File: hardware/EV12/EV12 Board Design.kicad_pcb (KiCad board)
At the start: 4 copper layers, 66 x 99.3 mm, 129 parts, among them CN2 Conn_05x02_Female, CN3 Conn_01x06_Female, CN4 Conn_01x06_Female, CN5 Conn_02x05_Male, CN6 Conn_02x05_Male, CN7 Conn_02x05_Male, J1 Conn_01x02_Socket, J10 Conn_01x08_Socket, J2 AudioJack1, J3 Conn_01x06_Socket, J9 USB_C_Receptacle, SW1 TS-1037-A11B3-D2, SW3 TS-1037-A11B3-D2, SW4 SW_Push, SW5 SW_Push, SW6 SW_SPDT, U1 STM32F405RGTx, U11 ESP32-S3-WROOM-1-N8R2, U13 BM14B(0.8)-24DS-0.4V(53), U2 BQ21040DBV, U3 CH340C, U4 USBLC6-2P6, U5 M24C02-RMN6TP, U6 WM8960CGEFL/RV, U7 TPS63060, U8 STM32F072CBTx, Y1 Crystal_GND24

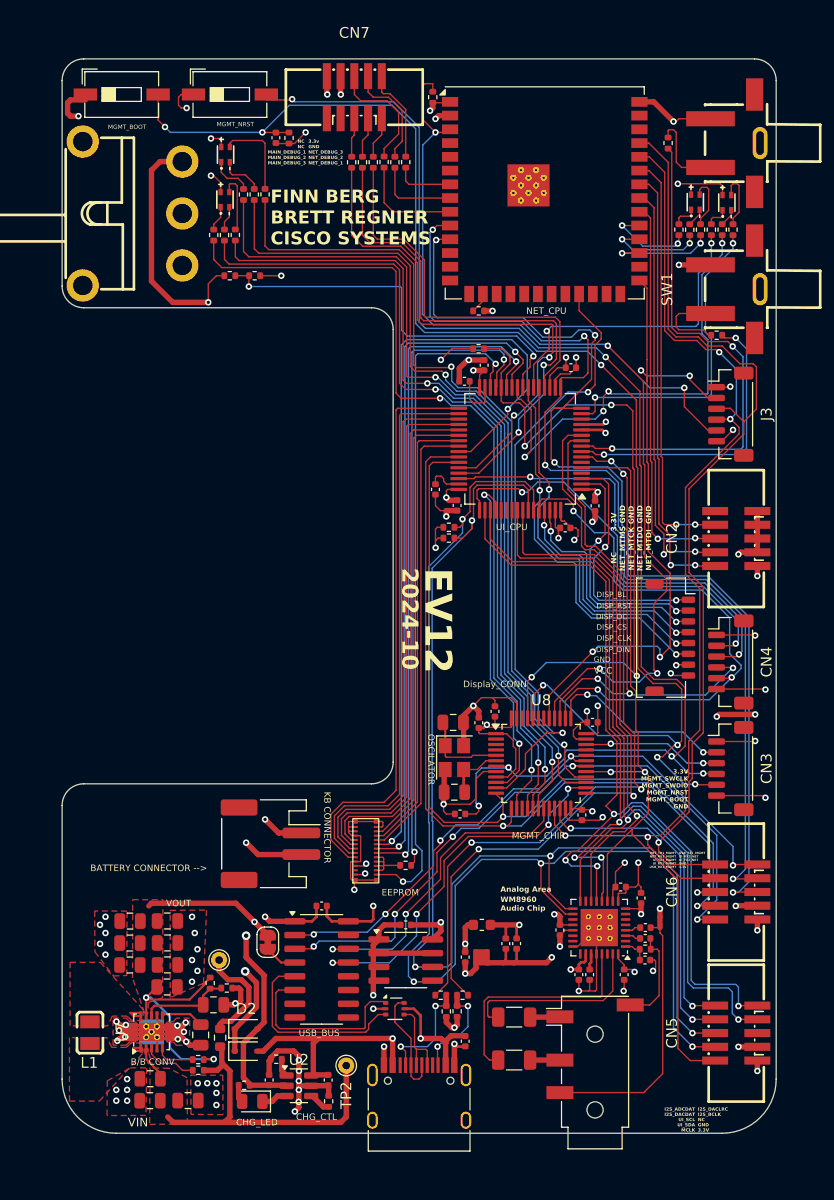
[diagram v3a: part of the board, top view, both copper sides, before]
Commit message: Added some design rules, updated track widths to be between 5 to 15mils except for long power lines
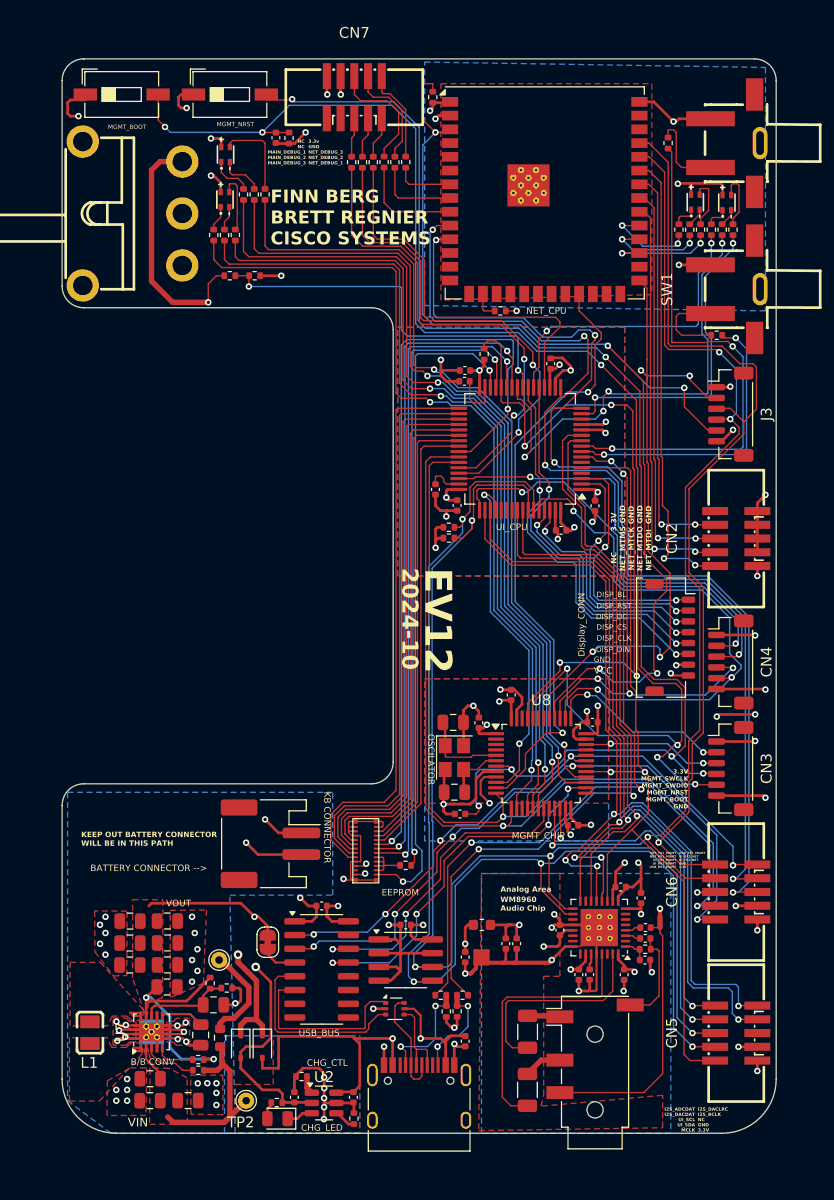
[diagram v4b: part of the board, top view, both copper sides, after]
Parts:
- moved TP2 9.80 mm to (131.0, 142.3)
- moved R27 3.41 mm to (133.8, 142.5)
- moved C29 3.02 mm to (157.0, 141.3), turned to 90 degrees
- moved R22 2.83 mm to (136.1, 140.1)
- moved D1 2.83 mm to (133.9, 144.0)
- moved C2 2.83 mm to (135.5, 142.0)
- moved C21 2.83 mm to (140.9, 142.0)
- moved R26 2.83 mm to (141.0, 143.9)
- moved U2 2.83 mm to (138.2, 142.5)
- moved C26 2.14 mm to (155.5, 104.8)
- moved R32 2.00 mm to (154.5, 69.3)
- moved C11 1.91 mm to (159.2, 74.2), turned to 90 degrees
- moved C14 1.84 mm to (151.2, 74.8), turned to 180 degrees
- moved C30 1.84 mm to (157.0, 135.9), turned to 90 degrees
- moved D2 1.72 mm to (130.5, 137.3), turned to -90 degrees
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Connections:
- CN2 pad 2: /NET_MTDI -> /NET_MTMS
- CN2 pad 4: /NET_MTDO -> /NET_MTCK
- CN2 pad 6: /NET_MTCK -> /NET_MTDO
- CN2 pad 8: /NET_MTMS -> /NET_MTDI
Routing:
- net Net-(U7-VIN): track 34.8 -> 20.7 mm
- net /UI_DEBUG_1: track 49.6 -> 44.3 mm
- net VBUS: track 33.7 -> 38.6 mm
- net Net-(D2-A): track 33.0 -> 37.7 mm
- net GNDA: track 70.7 -> 75.2 mm, vias 7 -> 8
- net /UI_DEBUG_2: track 49.6 -> 45.2 mm
- net /NET_MTMS: track 38.9 -> 42.5 mm
- net /NET_MTDI: track 41.0 -> 37.8 mm
- net Net-(U6-HP_R): track 21.5 -> 24.8 mm
- net GND: track 615.6 -> 618.5 mm
- net /MGMT_BOOT: track 134.0 -> 136.8 mm
- net /NET_RX1_MGMT: track 95.1 -> 97.7 mm
- net /NET_TX1_MGMT: track 98.0 -> 100.0 mm
- net Net-(U6-HP_L): track 17.7 -> 19.6 mm
- net /KB_ROW7: track 63.4 -> 61.9 mm
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- added copper zone on B.Cu, net GND
- added copper zone on B.Cu, net GNDA
- added copper zone on F.Cu, net GNDA
